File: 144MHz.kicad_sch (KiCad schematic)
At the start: 45 parts, among them J4 BWSMA-KWE-Z001, U5 GRF5604, U6 SKYA21003

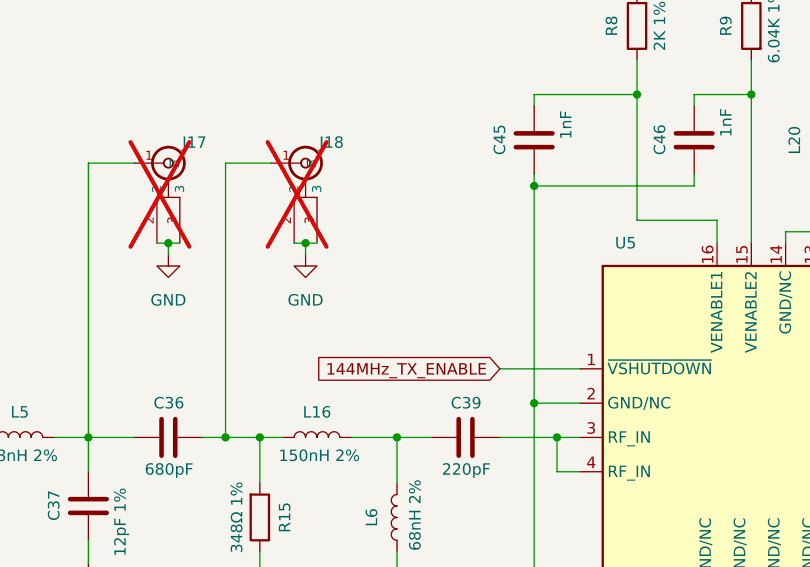
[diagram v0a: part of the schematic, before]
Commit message: Add pull up on the PA enables
So they are off by default.

Signed-off-by: Corey Minyard <corey@minyard.net>
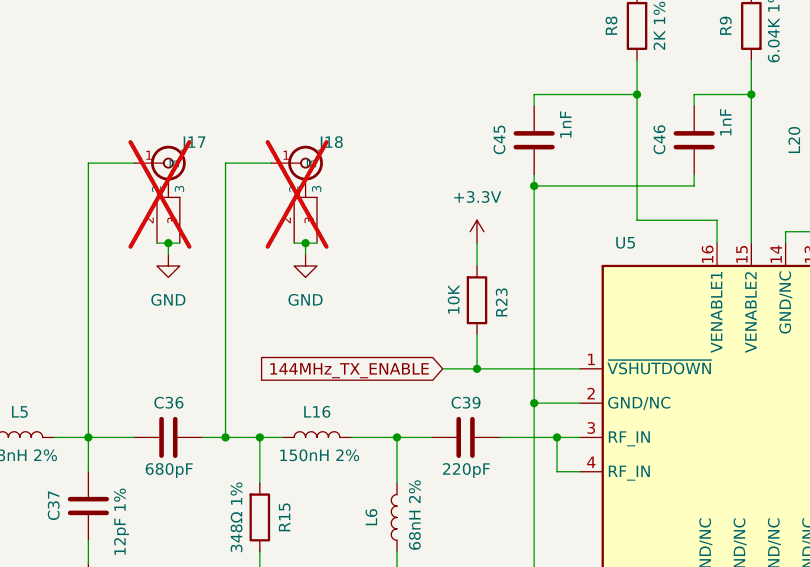
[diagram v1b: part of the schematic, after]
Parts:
- added R23: 10K, Resistor_SMD:R_0402_1005Metric, symbol Device:R
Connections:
- net +3.3V: now also R23.2
- net 144MHz_TX_ENABLE: now also R23.1
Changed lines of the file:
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@@
 	)
 	(junction
+		(at 135.89 71.12)
+		(diameter 0)
+		(color 0 0 0 0)
+	)
+	(junction
 		(at 76.2 78.74)
 		(diameter 0)
@@
 	(wire
 		(pts
+			(xy 135.89 67.31) (xy 135.89 71.12)
+		)
+		(stroke
+			(width 0)
+			(type default)
+		)
+	)
+	(wire
+		(pts
 			(xy 33.02 54.61) (xy 33.02 78.74)
 		)
@@
 	(wire
 		(pts
+			(xy 135.89 57.15) (xy 135.89 59.69)
+		)
+		(stroke
+			(width 0)
+			(type default)
+		)
+	)
+	(wire
+		(pts
 			(xy 228.6 90.17) (xy 228.6 92.71)
 		)
@@
 	(wire
 		(pts
+			(xy 135.89 71.12) (xy 147.32 71.12)
+		)
+		(stroke
+			(width 0)
+			(type default)
+		)
+	)
+	(wire
+		(pts
 			(xy 185.42 55.88) (xy 193.04 55.88)
 		)
@@
 	(wire
 		(pts
-			(xy 138.43 71.12) (xy 147.32 71.12)
+			(xy 132.08 71.12) (xy 135.89 71.12)
 		)
 		(stroke
@@
 	(global_label "144MHz_TX_ENABLE"
 		(shape input)
-		(at 138.43 71.12 180)
+		(at 132.08 71.12 180)
 		(fields_autoplaced yes)
 		(effects
@@
 		)
 		(property "Intersheetrefs" "${INTERSHEET_REFS}"
-			(at 116.8788 71.12 0)
+			(at 110.5288 71.12 0)
 			(effects
 				(font
@@
 	)
 	(symbol
+		(lib_id "power:+12V")
+		(at 135.89 57.15 0)
+		(unit 1)
+		(exclude_from_sim no)
+		(in_bom yes)
+		(on_board yes)
+		(dnp no)
+		(fields_autoplaced yes)
+		(property "Reference" "#PWR0105"
+			(at 135.89 60.96 0)
+			(effects
+				(font
+					(size 1.27 1.27)
+				)
+				(hide yes)
+			)
+		)
+		(property "Value" "+3.3V"
+			(at 135.89 52.07 0)
+			(effects
+				(font
+					(size 1.27 1.27)
+				)
+			)
+		)
+		(property "Footprint" ""
+			(at 135.89 57.15 0)
+			(effects
+				(font
+					(size 1.27 1.27)
+				)
+				(hide yes)
+			)
+		)
+		(property "Datasheet" ""
+			(at 135.89 57.15 0)
+			(effects
+				(font
+					(size 1.27 1.27)
+				)
+				(hide yes)
+			)
+		)
+		(property "Description" "Power symbol creates a global label with name \"+12V\""
+			(at 135.89 57.15 0)
+			(effects
+				(font
+					(size 1.27 1.27)
+				)
+				(hide yes)
+			)
+		)
+		(pin "1"
+		)
+		(instances
+			(project "FSKGroundStation"
+				(path "/23e49ab9-97e0-460a-806c-ff6f37958474/09d49814-9bff-4ecc-b3ba-584a511e3f87"
+					(reference "#PWR0105")
+					(unit 1)
+				)
+			)
+		)
+	)
+	(symbol
 		(lib_id "power:GND")
 		(at 102.87 115.57 0)
@@
 					(unit 1)
 				)
+			)
+		)
+	)
+	(symbol
+		(lib_id "Device:R")
+		(at 135.89 63.5 0)
+		(mirror x)
+		(unit 1)
+		(exclude_from_sim no)
+		(in_bom yes)
+		(on_board yes)
+		(dnp no)
+		(property "Reference" "R23"
+			(at 138.684 63.754 90)
+			(effects
+				(font
+					(size 1.27 1.27)
+				)
+			)
+		)
+		(property "Value" "10K"
+			(at 133.35 63.5 90)
+			(effects
+				(font
+					(size 1.27 1.27)
+				)
+			)
+		)
+		(property "Footprint" "Resistor_SMD:R_0402_1005Metric"
+			(at 134.112 63.5 90)
+			(effects
+				(font
+					(size 1.27 1.27)
+				)
+				(hide yes)
+			)
+		)
+		(property "Datasheet" "~"
+			(at 135.89 63.5 0)
+			(effects
+				(font
+					(size 1.27 1.27)
+				)
+				(hide yes)
+			)
+		)
+		(property "Description" "Resistor"
+			(at 135.89 63.5 0)
+			(effects
+				(font
+					(size 1.27 1.27)
+				)
+				(hide yes)
+			)
+		)
+		(pin "2"
+		)
+		(pin "1"
+		)
+		(instances
+			(project "FSKGroundStation"
+				(path "/23e49ab9-97e0-460a-806c-ff6f37958474/09d49814-9bff-4ecc-b3ba-584a511e3f87"
+					(reference "R23")
+					(unit 1)
+				)

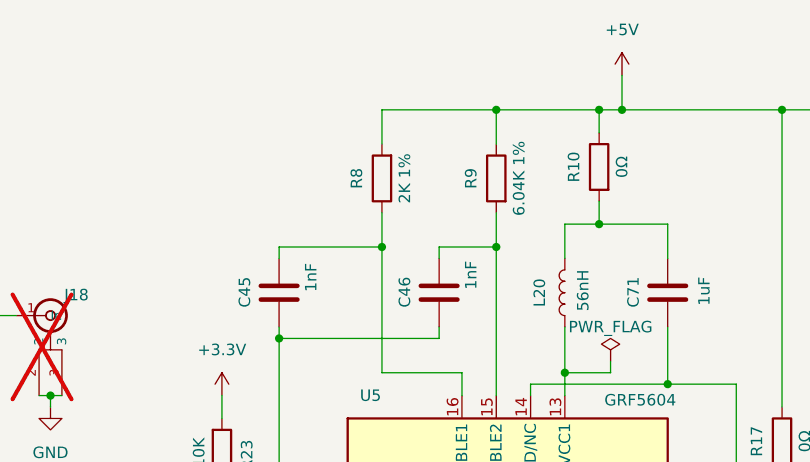
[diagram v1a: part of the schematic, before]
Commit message: Change a resistor on the 150MHz TX
No need to have a 2K and a 1.96K resistor for this, just use 1.96K
on both.

Signed-off-by: Corey Minyard <corey@minyard.net>
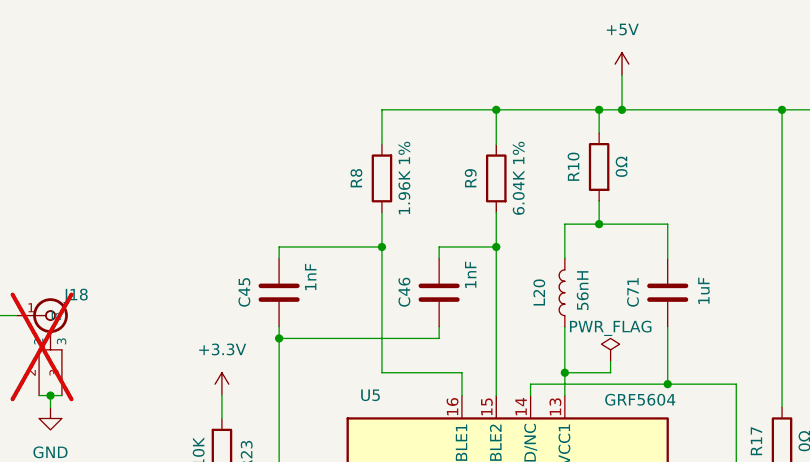
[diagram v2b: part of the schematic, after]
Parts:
- R8: value 2K 1% -> 1.96K 1%
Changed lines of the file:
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@@
 			)
 		)
-		(property "Value" "2K 1%"
+		(property "Value" "1.96K 1%"
 			(at 156.21 33.02 90)
 			(effects

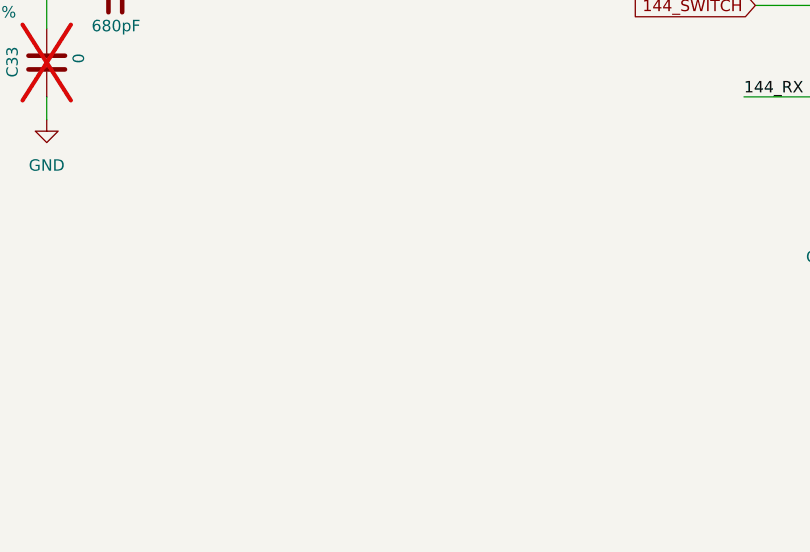
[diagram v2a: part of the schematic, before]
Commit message: Add thermsistors by the PAs
Signed-off-by: Corey Minyard <corey@minyard.net>
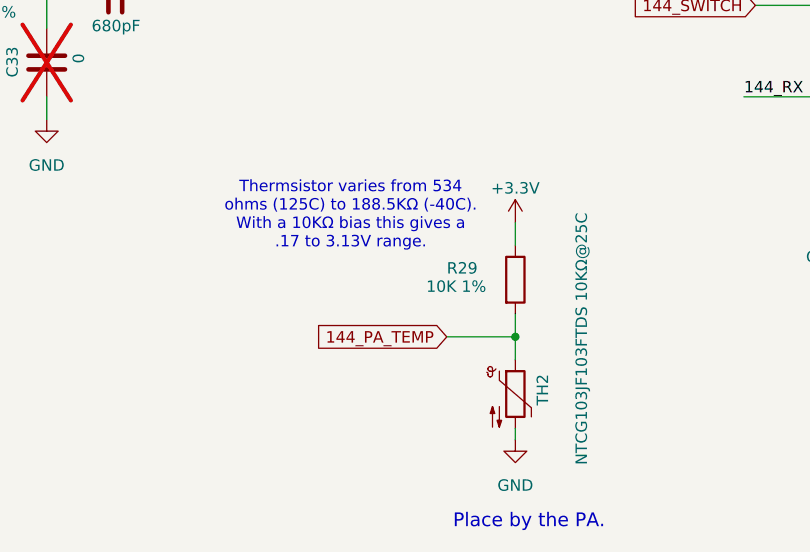
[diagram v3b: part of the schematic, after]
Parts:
- added R29: 10K 1%, Resistor_SMD:R_0402_1005Metric_Pad0.72x0.64mm_HandSolder, symbol Device:R
- added TH2: NTCG103JF103FTDS 10KΩ@25C, Resistor_SMD:R_0402_1005Metric, symbol Device:Thermistor_NTC
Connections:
- net +3.3V: now also R29.1
- net GND: now also TH2.2
- new net 144_PA_TEMP: R29.2, TH2.1
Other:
- note added: "Place by the PA."
- note added: "Thermsistor varies from 534 ohms (125C) to 188.5KΩ (-40C). With a 10KΩ bias this gives a .17 to 3.13V range."

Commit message: More re-layout for the new design
Signed-off-by: Corey Minyard <corey@minyard.net>
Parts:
- added C126: 2.2nF, Capacitor_SMD:C_0402_1005Metric_Pad0.74x0.62mm_HandSolder, symbol Device:C
- added L28, L29: 82nH 2%, Inductor_SMD:L_0603_1608Metric_Pad1.05x0.95mm_HandSolder, symbol Device:L
- added L31: 39nH 2%, Inductor_SMD:L_0402_1005Metric_Pad0.77x0.64mm_HandSolder, symbol Device:L
- C31: value 18pF 1% -> 12pF 1%
- C32, C73: value 680pF -> 12pF 1%
- C33: value 0 -> 1nF
- C34: value 18pF 1% -> 15pF 1%
- C35: value 33pF 1% -> 1.2pF
- L1: value 150nH -> 18nH 2%; footprint Inductor_SMD:L_0805_2012Metric_Pad1.05x1.20mm_HandSolder -> Inductor_SMD:L_0402_1005Metric_Pad0.77x0.64mm_HandSolder
- L3: value 82nH 2% -> 100nH 2%
- L4: value 47nH 2% -> 68nH 2%
- L5: value 68nH 2% -> 150nH
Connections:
- net 144MHz_RX_TX is gone; now on an unnamed net: C30.2, L1.1
- net 144_RX: now also U6.5 (RF3), C126.2; no longer C32.2, U6.11 (RF2)
- net 144_TX: now also U6.11 (RF2); no longer U6.5 (RF3)
- net GND: now also C32.1, L28.1; no longer C30.1, C31.1, C33.1, C35.1
- net at C35.2, L4.2: now also C36.1, J17.1 (In); no longer L5.1
- net 144_RF_N: now reaches C37.2, L5.2
- net 144_RF_N: now also L29.1; no longer C36.1, J17.1 (In)
- net at C33.2, L3.2: now also C34.2, C35.1, L4.1; no longer C32.1, J16.1 (In)
- net 144MHz_RF_N: no longer names the net of J7.1 (In)
- net 144MHz_RF_N: now also C31.1; no longer C73.1
- net 144MHz_RF_P: no longer names the net of C31.2, L1.2, L3.1
- net 144MHz_RF_P: now also C32.2
- new net: C73.2, L29.2, L31.1
- new net: C126.1, J16.1 (In), L31.2
- new net 144_PA: C30.1, J6.1 (In)
- new net 144_RF_P: C73.1, L28.2, L5.1
- new net 144_TRX_SW: C33.1

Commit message: Add some vias
Signed-off-by: Corey Minyard <corey@minyard.net>
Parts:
- L5: footprint Inductor_SMD:L_0603_1608Metric_Pad1.05x0.95mm_HandSolder -> Inductor_SMD:L_0805_2012Metric_Pad1.05x1.20mm_HandSolder
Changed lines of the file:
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@@
 			)
 		)
-		(property "Footprint" "Inductor_SMD:L_0603_1608Metric_Pad1.05x0.95mm_HandSolder"
+		(property "Footprint" "Inductor_SMD:L_0805_2012Metric_Pad1.05x1.20mm_HandSolder"
 			(at 43.18 143.51 0)
 			(effects

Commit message: Add some LEDs
Signed-off-by: Corey Minyard <corey@minyard.net>
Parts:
- TH2: value NTCG103JF103FTDS 10KΩ@25C -> Thermistor_NTC
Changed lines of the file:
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@@
 			)
 		)
-		(property "Value" "NTCG103JF103FTDS 10KΩ@25C"
+		(property "Value" "Thermistor_NTC"
 			(at 149.606 180.594 90)
 			(effects
@@
 			)
 		)
-		(property "Datasheet" "NCU15XH103F60RC"
+		(property "Datasheet" "~"
 			(at 142.24 171.45 0)
 			(effects

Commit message: Fix some components messed up by the previous change
Signed-off-by: Corey Minyard <corey@minyard.net>
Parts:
- TH2: value Thermistor_NTC -> NTCG103JF103FTDS 10KΩ@25C
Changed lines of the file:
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@@
 			)
 		)
-		(property "Value" "Thermistor_NTC"
-			(at 149.606 180.594 90)
+		(property "Value" "NTCG103JF103FTDS 10KΩ@25C"
+			(at 147.32 183.134 90)
 			(effects
 				(font
